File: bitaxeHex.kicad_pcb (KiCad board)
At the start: 4 copper layers, 84.5 x 129.5 mm, 363 parts, among them J1 XT30, J3 Conn_02x05_Odd_Even, J4 TC2030-IDC, J5 Conn_01x04, J6 Conn_01x06, J7 USB_C_Receptacle_USB2.0, J8 Conn_01x04, J9 Conn_01x04, SW1 SWITCH-SPST, SW2 SWITCH-SPST, U1 LMR54410, U10 SGM2036-0v8, U11 SGM2036-1v8, U12 BM1366_mode1, U13 BM1366_mode1, U14 25MHz, U15 TLV3544, U16 SGM2036-1v8, U17 SGM2036-0v8, U18 BM1366_mode0, U19 25MHz, U2 RT9080-33GJ5, U20 BM1366_mode0, U21 TLV3544, U22 BM1366_mode1, U23 SGM2036-0v8, U24 SGM2036-1v8, U25 BM1366_mode1, U26 25MHz, U3 TPS546D24ARVFR, U4 MIC5504, U5 SN74AVC4T774, U6 ESP32-S3-WROOM-1, U7 TMP1075, U8 TMP1075, U9 EMC2302, Y1 32.768kHz

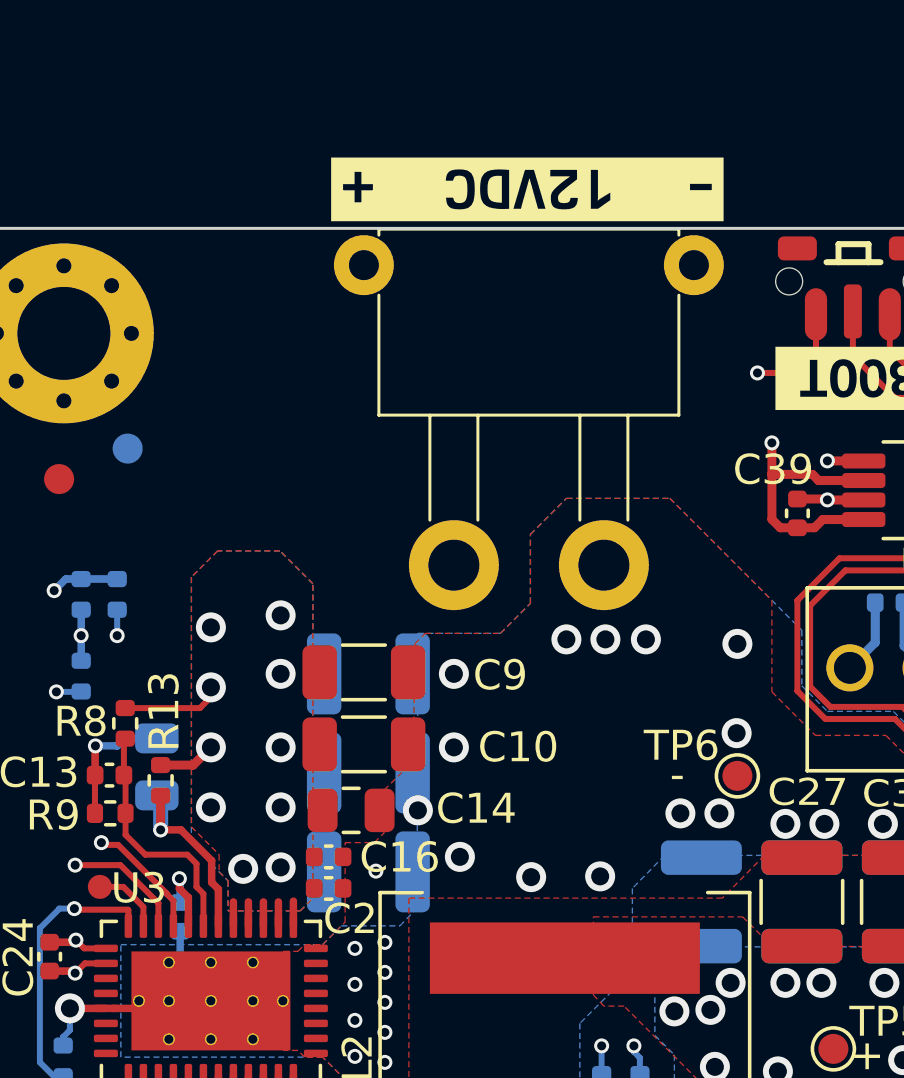
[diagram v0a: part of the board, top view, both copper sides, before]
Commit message: add XT30 3D model
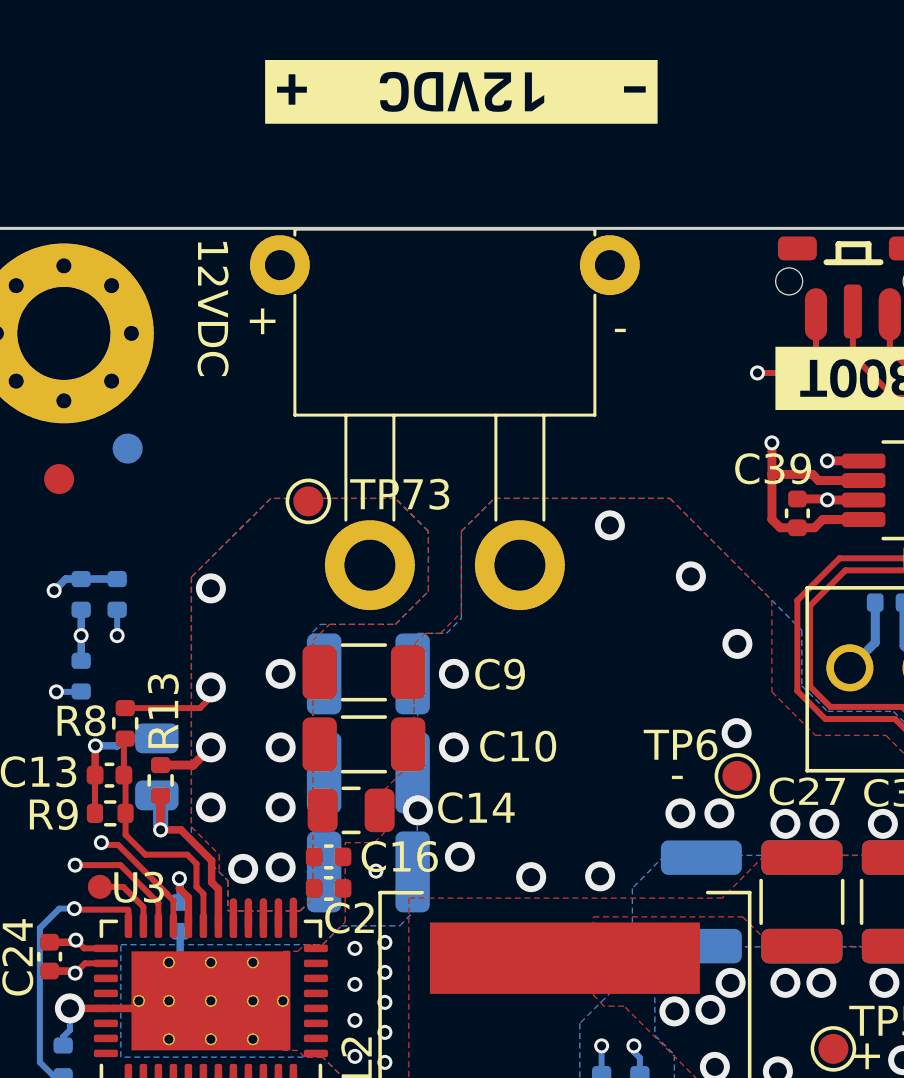
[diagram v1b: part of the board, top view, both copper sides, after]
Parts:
- added TP73: TestPoint, TestPoint:TestPoint_Pad_D1.0mm, F.Cu at (61.6, 55.1)
- moved kibuzzard-65978662 3.92 mm to (66.8, 41.5)
- moved J1 2.80 mm to (66.2, 57.2)
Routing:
- net /VIN: track 111.0 -> 104.9 mm, vias 13 -> 12
- net GND: vias 109 -> 108
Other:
- board text added: "12VDC"
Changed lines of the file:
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@@
 	(footprint "bitaxe:XT30PW-M"
 		(layer "F.Cu")
-		(at 69 57.225)
+		(at 66.2 57.225)
 		(property "Reference" "J1"
 			(at -0.69 2.21 0)
@@
 			)
 		)
-		(property ki_fp_filters "Connector*:*_1x??_*")
-		(sheetname "Root")
-		(sheetfile "bitaxeHex.kicad_sch")
 		(attr smd)
 		(fp_line
@@
 			(net 55 "/VIN")
 			(pinfunction "+V")
-			(pintype "passive")
-			(zone_connect 0)
+			(pintype "power_in")
 		)
 		(pad "2" thru_hole circle
@@
 			(net 1 "GND")
 			(pinfunction "GND")
-			(pintype "passive")
-			(zone_connect 0)
+			(pintype "power_in")
+			(zone_connect 2)
 		)
 		(pad "3" thru_hole circle
@@
 		)
 	)
+	(footprint "TestPoint:TestPoint_Pad_D1.0mm"
+		(layer "F.Cu")
+		(at 61.65 55.1)
+		(descr "SMD pad as test Point, diameter 1.0mm")
+		(tags "test point SMD pad")
+		(property "Reference" "TP73"
+			(at 3.1 -0.2 0)
+			(layer "F.SilkS")
+			(effects
+				(font
+					(size 1 1)
+					(thickness 0.15)
+				)
+			)
+		)
+		(property "Value" "TestPoint"
+			(at 4.2 1.2 0)
+			(layer "F.Fab")
+			(effects
+				(font
+					(size 1 1)
+					(thickness 0.15)
+				)
+			)
+		)
+		(property "Footprint" "TestPoint:TestPoint_Pad_D1.0mm"
+			(at 0 0 0)
+			(unlocked yes)
+			(layer "F.Fab")
+			(hide yes)
+			(effects
+				(font
+					(size 1.27 1.27)
+				)
+			)
+		)
+		(property "Datasheet" ""
+			(at 0 0 0)
+			(unlocked yes)
+			(layer "F.Fab")
+			(hide yes)
+			(effects
+				(font
+					(size 1.27 1.27)
+				)
+			)
+		)
+		(property "Description" ""
+			(at 0 0 0)
+			(unlocked yes)
+			(layer "F.Fab")
+			(hide yes)
+			(effects
+				(font
+					(size 1.27 1.27)
+				)
+			)
+		)
+		(property ki_fp_filters "Pin* Test*")
+		(sheetname "Root")
+		(sheetfile "bitaxeHex.kicad_sch")
+		(attr exclude_from_pos_files exclude_from_bom)
+		(fp_circle
+			(center 0 0)
+			(end 0 0.7)
+			(stroke
+				(width 0.12)
+				(type solid)
+			)
+			(fill none)
+			(layer "F.SilkS")
+		)
+		(fp_circle
+			(center 0 0)
+			(end 1 0)
+			(stroke
+				(width 0.05)
+				(type solid)
+			)
+			(fill none)
+			(layer "F.CrtYd")
+		)
+		(fp_text user "${REFERENCE}"
+			(at 0 -1.45 0)
+			(layer "F.Fab")
+			(effects
+				(font
+					(size 1 1)
+					(thickness 0.15)
+				)
+			)
+		)
+		(pad "1" smd circle
+			(at 0 0)
+			(size 1 1)
+			(layers "F.Cu" "F.Mask")
+			(net 55 "/VIN")
+			(pinfunction "1")
+			(pintype "passive")
+		)
+	)
 	(footprint "Capacitor_SMD:C_0805_2012Metric"
 		(layer "F.Cu")
@@
 	(footprint "kibuzzard-65978662"
 		(layer "F.Cu")
-		(at 68.95 44.7 180)
+		(at 66.75 41.45 180)
 		(descr "Generated with KiBuzzard")
 		(tags "kb_params=eyJBbGlnbm1lbnRDaG9pY2UiOiAiQ2VudGVyIiwgIkNhcExlZnRDaG9pY2UiOiAiWyIsICJDYXBSaWdodENob2ljZSI6ICJdIiwgIkZvbnRDb21ib0JveCI6ICJCZXJrZWxleU1vbm8tQm9sZCIsICJIZWlnaHRDdHJsIjogIjEuMiIsICJMYXllckNvbWJvQm94IjogIkYuU2lsa1MiLCAiTXVsdGlMaW5lVGV4dCI6ICItICAxMlZEQyAgKyIsICJQYWRkaW5nQm90dG9tQ3RybCI6ICI1IiwgIlBhZGRpbmdMZWZ0Q3RybCI6ICI1IiwgIlBhZGRpbmdSaWdodEN0cmwiOiAiNSIsICJQYWRkaW5nVG9wQ3RybCI6ICI1IiwgIldpZHRoQ3RybCI6ICIifQ==")
@@
 		)
 		(property "Value" "0.1uF"
-			(at 0 -1.16 360)
+			(at 0 -1.16 0)
 			(layer "B.Fab")
 			(effects
@@
 		)
 		(property "DK" "478-KGM05AR71C104KHCT-ND"
-			(at 0 0 360)
+			(at 0 0 0)
 			(layer "B.Fab")
 			(hide yes)
@@
 		)
 		(property "PARTNO" "KGM05AR71C104KH"
-			(at 0 0 360)
+			(at 0 0 0)
 			(layer "B.Fab")
 			(hide yes)
@@
 		)
 		(fp_text user "${REFERENCE}"
-			(at 0 0 360)
+			(at 0 0 0)
 			(layer "B.Fab")
 			(effects
@@
 	)
 	(gr_text "-"
+		(at 71.8 49.9 0)
+		(layer "F.SilkS")
+		(effects
+			(font
+				(size 1 1)
+				(thickness 0.15)
+			)
+			(justify left bottom)
+		)
+	)
+	(gr_text "-"
 		(at 73.7 64.8 0)
 		(layer "F.SilkS")
@@
 		)
 	)
+	(gr_text "12VDC"
+		(at 57.85 46.3 -90)
+		(layer "F.SilkS")
+		(effects
+			(font
+				(size 1 1)
+				(thickness 0.15)
+			)
+			(justify left bottom)
+		)
+	)
+	(gr_text "+"
+		(at 59.55 49.65 0)
+		(layer "F.SilkS")
+		(effects
+			(font
+				(size 1 1)
+				(thickness 0.15)
+			)
+			(justify left bottom)
+		)
+	)
 	(gr_text "Slide rail clearance"
 		(at 133.4 165.2 90)
@@
 	)
 	(via
-		(at 70.25 59.7)
-		(size 1)
-		(drill 0.6)
-		(layers "F.Cu" "B.Cu")
-		(free yes)
-		(net 1)
-	)
-	(via
 		(at 65.3 65.4)
 		(size 1)
@@
 	)
 	(via
-		(at 72.9 59.7)
+		(at 74.4 57.6)
 		(size 1)
 		(drill 0.6)
@@
 	)
 	(via
-		(at 71.55 59.7)
+		(at 71.7 55.9)
 		(size 1)
 		(drill 0.6)
@@
 	)
 	(via
-		(at 58.4 59.3)
-		(size 1)
-		(drill 0.6)
-		(layers "F.Cu" "B.Cu")
-		(free yes)
-		(net 55)
-	)
-	(via
 		(at 58.4 65.3)
 		(size 1)
@@
 	)
 	(via
-		(at 60.725 58.9)
+		(at 58.4 58)
 		(size 1)
 		(drill 0.6)
@@
 	)
 	(segment
+		(start 63.7 57.225)
+		(end 63.7 53.4)
+		(width 2)
+		(layer "In1.Cu")
+		(net 55)
+	)
+	(segment
 		(start 87.45 69.7)
 		(end 87.45 72.375)
@@
 	)
 	(segment
-		(start 77.55 56.55)
-		(end 82.2 56.55)
-		(width 2)
-		(layer "In1.Cu")
-		(net 55)
-	)
-	(segment
 		(start 82.24 61.64)
 		(end 84.35 63.75)
@@
 	)
 	(segment
-		(start 71.25 50.25)
-		(end 77.55 56.55)
-		(width 2)
-		(layer "In1.Cu")
-		(net 55)
-	)
-	(segment
 		(start 84.35 66.6)
 		(end 87.45 69.7)
@@
 	)
 	(segment
+		(start 65.15 51.95)
+		(end 72.6 51.95)
+		(width 2)
+		(layer "In1.Cu")
+		(net 55)
+	)
+	(segment
 		(start 84.35 63.75)
 		(end 84.35 66.6)
@@
 	)
 	(segment
-		(start 59.95 51.9)
-		(end 61.6 50.25)
+		(start 72.6 51.95)
+		(end 77.2 56.55)
 		(width 2)
 		(layer "In1.Cu")
@@
 	)
 	(segment
-		(start 61.6 50.25)
-		(end 71.25 50.25)
+		(start 63.7 53.4)
+		(end 65.15 51.95)
+		(width 2)
+		(layer "In1.Cu")
+		(net 55)
+	)
+	(segment
+		(start 77.2 56.55)
+		(end 82.2 56.55)
 		(width 2)
 		(layer "In1.Cu")
@@
 	)
 	(segment
-		(start 59.95 51.9)
-		(end 59.95 57.3)
-		(width 2)
-		(layer "In1.Cu")
-		(net 55)
-	)
-	(segment
 		(start 87.45 73.725)
 		(end 87.45 72.375)
@@
 				(xy 62.9 74.4) (xy 62.125 73.625) (xy 61.525 73.625) (xy 61.3 73.4) (xy 60.825 73.4) (xy 60.825 70.1)
 				(xy 61.3 70.1) (xy 61.525 69.875) (xy 62.125 69.875) (xy 62.875 69.125) (xy 62.875 66.475) (xy 63.85 66.475)
-				(xy 64.175 66.15) (xy 64.175 64.725) (xy 65.15 63.75) (xy 65.2 59.85) (xy 65.55 59.5) (xy 68.05 59.5)
-				(xy 69.05 58.5) (xy 69.05 56.2) (xy 70.25 55) (xy 73.7 55) (xy 77.1 58.4) (xy 77.1 61.45) (xy 78.55 62.9)
+				(xy 64.175 66.15) (xy 64.175 64.725) (xy 65.15 63.75) (xy 65.2 59.85) (xy 65.55 59.5) (xy 66.05 59.5)
+				(xy 66.75 58.8) (xy 66.75 56.1) (xy 67.85 55) (xy 73.7 55) (xy 77.1 58.4) (xy 77.1 61.45) (xy 78.55 62.9)
 				(xy 80.9 62.9) (xy 82.85 64.85) (xy 82.85 66.9) (xy 76.85 66.9) (xy 75.45 68.325) (xy 65 68.325)
 				(xy 65 74.4)
@@
 		(polygon
 			(pts
-				(xy 61.375 68.75) (xy 61.8 68.325) (xy 61.8 57.85) (xy 60.7 56.75) (xy 58.625 56.75) (xy 57.75 57.625)
-				(xy 57.75 65.95) (xy 58.675 66.875) (xy 58.675 67.45) (xy 58.975 67.75) (xy 58.975 68.75)
+				(xy 61.375 68.75) (xy 61.8 68.325) (xy 61.8 59.75) (xy 62.35 59.2) (xy 64.55 59.2) (xy 65.65 58.1)
+				(xy 65.65 56.1) (xy 64.55 55) (xy 60.4 55) (xy 57.75 57.625) (xy 57.75 65.95) (xy 58.675 66.875)
+				(xy 58.675 67.45) (xy 58.975 67.75) (xy 58.975 68.75)
 			)
 		)
@@
 			(pts
 				(xy 104.55 66.25) (xy 109.9 71.6) (xy 109.9 80.3) (xy 114.95 85.325) (xy 134 85.325) (xy 134 51.4)
-				(xy 129.1 46.5) (xy 76.4 46.4) (xy 76.4 52.9) (xy 78.7 55.2) (xy 84.9 55.2) (xy 86.05 54.05) (xy 90.275 54.05)
+				(xy 129.1 46.5) (xy 76.4 46.4) (xy 76.4 52.9) (xy 78.5 55) (xy 85.1 55) (xy 86.05 54.05) (xy 90.275 54.05)
 				(xy 102.45 66.2)
 			)
@@
 		(hatch edge 0.5)
 		(priority 32)
-		(connect_pads
+		(connect_pads yes
 			(clearance 0)
 		)
@@
 		(polygon
 			(pts
-				(xy 58.65 56.725) (xy 60.7 56.725) (xy 62.05 58.05) (xy 62.05 65.65) (xy 62.85 66.45) (xy 62.85 67.95)
-				(xy 58.6 67.95) (xy 58.6 67.35) (xy 57.75 66.5) (xy 57.725 57.625)
+				(xy 60.35 55) (xy 64.55 55) (xy 65.65 56.1) (xy 65.65 58.1) (xy 64.55 59.2) (xy 62.35 59.2) (xy 62.05 59.5)
+				(xy 62.05 65.65) (xy 62.85 66.45) (xy 62.85 67.95) (xy 58.6 67.95) (xy 58.6 67.35) (xy 57.75 66.5)
+				(xy 57.725 57.625)
 			)
 		)
@@
 		(hatch edge 0.5)
 		(priority 34)
-		(connect_pads
+		(connect_pads yes
 			(clearance 0)
 		)
@@
 		(polygon
 			(pts
-				(xy 63.45 68.1) (xy 63.45 66.475) (xy 66.5 63.425) (xy 66.5 59.5) (xy 68.05 59.5) (xy 69.05 58.5)
-				(xy 69.05 56.2) (xy 70.25 55) (xy 73.7 55) (xy 77.1 58.4) (xy 77.1 61.45) (xy 78.55 62.9) (xy 80.9 62.9)
-				(xy 82.85 64.85) (xy 82.85 66.9) (xy 76.85 66.9) (xy 75.65 68.1)
+				(xy 63.45 68.1) (xy 63.45 66.475) (xy 66.05 63.875) (xy 66.05 59.5) (xy 66.75 58.8) (xy 66.75 56.1)
+				(xy 67.85 55) (xy 73.25 55) (xy 77.1 58.85) (xy 77.1 61.45) (xy 78.55 62.9) (xy 80.9 62.9) (xy 82.85 64.85)
+				(xy 82.85 66.9) (xy 76.85 66.9) (xy 75.65 68.1)
 			)
 		)
@@
 		(polygon
 			(pts
-				(xy 61.375 68.75) (xy 61.8 68.325) (xy 61.8 57.85) (xy 60.7 56.75) (xy 58.625 56.75) (xy 57.75 57.625)
-				(xy 57.75 66.525) (xy 58.975 67.75) (xy 58.975 68.75)
+				(xy 61.375 68.75) (xy 61.8 68.325) (xy 61.8 59.45) (xy 62.05 59.2) (xy 64.55 59.2) (xy 65.65 58.1)
+				(xy 65.65 56.1) (xy 64.55 55) (xy 60.4 55) (xy 57.75 57.625) (xy 57.75 66.525) (xy 58.975 67.75)
+				(xy 58.975 68.75)
 			)
 		)
@@
 			(pts
 				(xy 62.125 73.625) (xy 55.4 73.625) (xy 55.4 69.875) (xy 62.125 69.875) (xy 62.75 69.25) (xy 64.7 69.25)
-				(xy 65.275 68.65) (xy 65.3 59.5) (xy 68.05 59.5) (xy 69.05 58.5) (xy 69.05 56.2) (xy 70.25 55) (xy 73.7 55)
+				(xy 65.275 68.65) (xy 65.3 59.5) (xy 66.25 59.5) (xy 66.75 59) (xy 66.75 56.1) (xy 67.85 55) (xy 73.7 55)
 				(xy 78.1 59.4) (xy 78.1 61.25) (xy 78.95 62.1) (xy 81.15 62.1) (xy 82.85 63.8) (xy 82.85 66.9) (xy 73.525 66.9)
 				(xy 72.45 68) (xy 72.45 70.75) (xy 70.7 72.5) (xy 70.7 80.1) (xy 69.95 80.85) (xy 65.45 80.85) (xy 64.95 80.35)

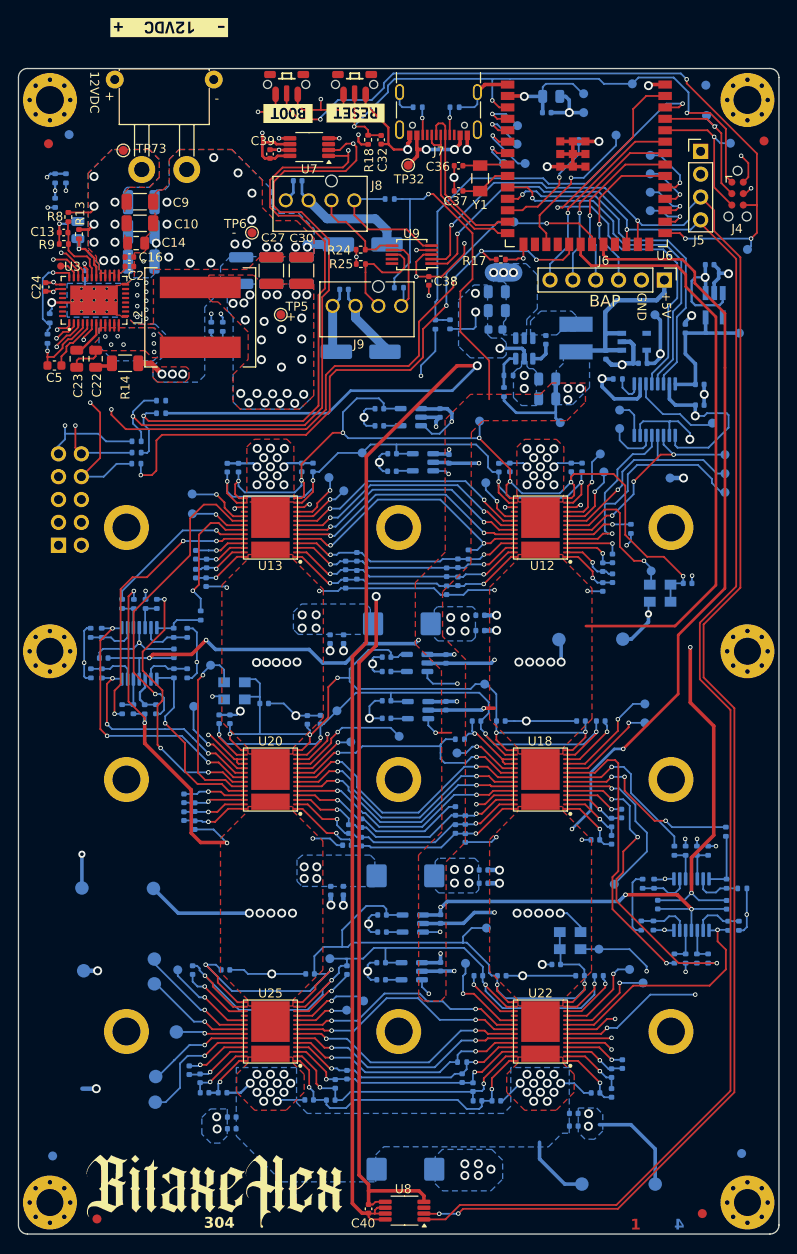
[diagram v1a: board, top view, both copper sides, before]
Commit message: add resistor dividers to domain voltage sense signals
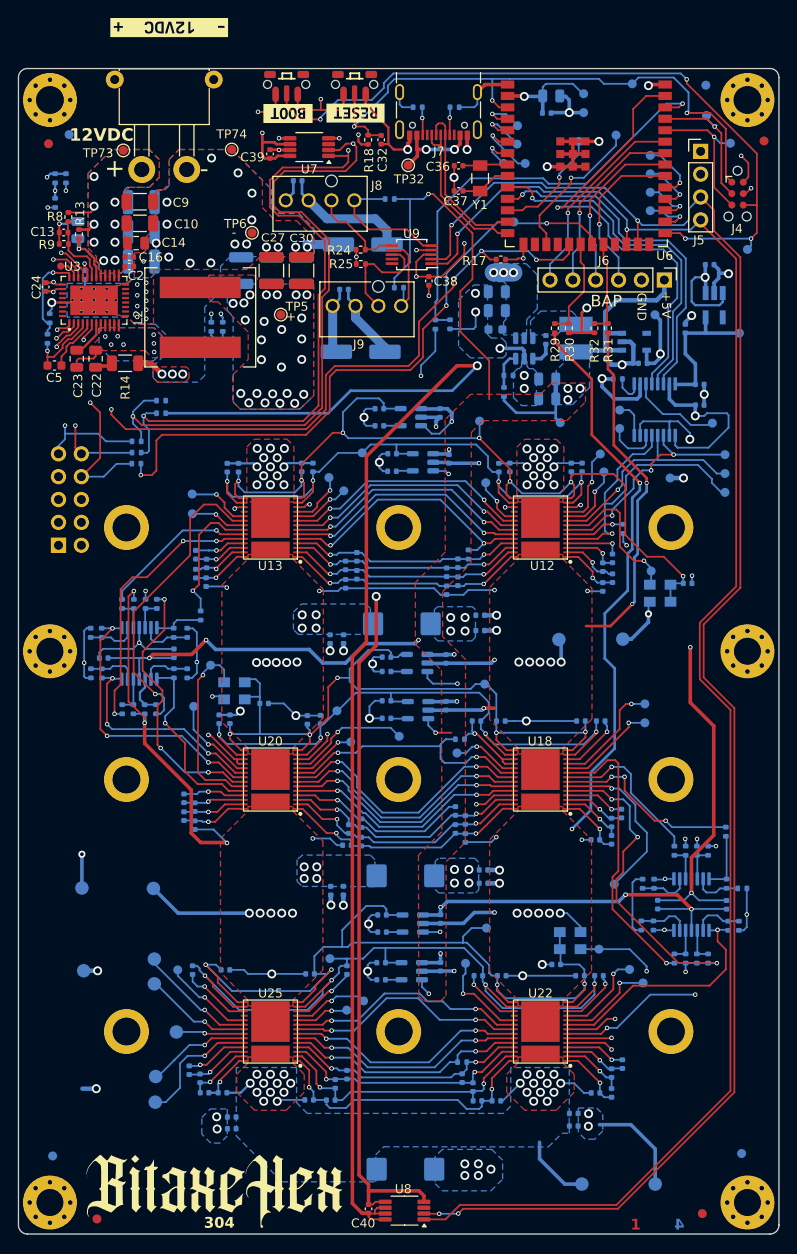
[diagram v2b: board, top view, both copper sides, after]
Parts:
- added R29: 7.87k, Resistor_SMD:R_0402_1005Metric, F.Cu at (109.6, 74.8)
- added R30: 22.1k, Resistor_SMD:R_0402_1005Metric, F.Cu at (111.2, 74.8)
- added R31: 7.87k, Resistor_SMD:R_0402_1005Metric, F.Cu at (115.5, 74.8)
- added R32: 22.1k, Resistor_SMD:R_0402_1005Metric, F.Cu at (114.0, 74.8)
- added TP74: TestPoint, TestPoint:TestPoint_Pad_D1.0mm, F.Cu at (73.7, 55.0)
- moved R28 0.85 mm to (117.2, 97.2)
- moved C31 0.05 mm to (109.2, 49.0)
- moved C33 0.05 mm to (108.7, 51.0)
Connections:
- net /ESP32/VDD_SAMPLE renamed /ESP32/VDD3_SAMPLE
- U6 pad 20: /VDD1 -> /ESP32/VDD2_SAMPLE
- U6 pad 22: /VDD2 -> /ESP32/VDD1_SAMPLE
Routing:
- net /VDD1: track 224.5 -> 197.3 mm, vias 46 -> 48
- net /VDD2: track 285.1 -> 265.1 mm
- net /ESP32/VDD2_SAMPLE: track 0.00 -> 11.2 mm
- net /ESP32/VDD1_SAMPLE: track 0.00 -> 10.5 mm
- net GND: track 348.4 -> 354.2 mm, vias 108 -> 109
- net /BM1366-1/BI1: track 7.60 -> 6.75 mm
- net /RO: track 24.3 -> 24.8 mm

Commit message: Clean up DRC errors vor v304
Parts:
- removed kibuzzard-65978662: G***, kibuzzard-65978662
- TP35, TP36, TP45, TP46, TP54, TP55, TP70, TP71, TP72: footprint TestPoint:TestPoint_Pad_D1.0mm -> bitaxe:TestPoint_Pad_D1.0mm_highlight
- moved U8 0.05 mm to (92.8, 172.9)
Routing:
- net /VDD2: track 265.1 -> 263.6 mm, vias 51 -> 50
